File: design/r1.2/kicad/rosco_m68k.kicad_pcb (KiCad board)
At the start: 4 copper layers, 160 x 100 mm, 81 parts, among them IC1 MC68010P10, IC2 ATF16V8BQL-15PU, IC3 ATF16V8BQL, IC4 MC68901P, IC5 ATF16V8BQL, IC6 74174N, IC7 74LS93, IC8 555N, IC9 74LS01N, J1 PWR, J2 Conn_01x06, J3 Conn_02x32_Odd_Even, J5 GPIO-PANEL, Q1 3.6864MHz, Q2 5H8ET-10.000, Q3 5H8ET-4.000, U1 AT28C256-15PU, U2 AT28C256-15PU, U3 AS6C4008-55PCN, U4 AS6C4008-55PCN

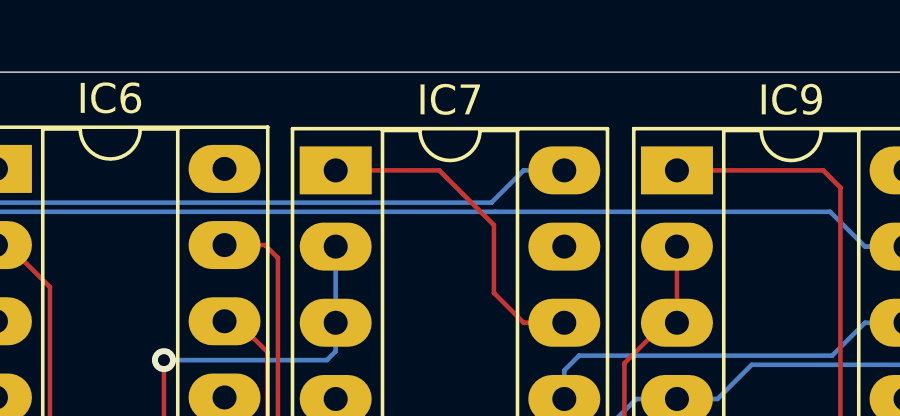
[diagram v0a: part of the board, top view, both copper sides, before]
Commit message: Rerate LED limiters for new LED stock
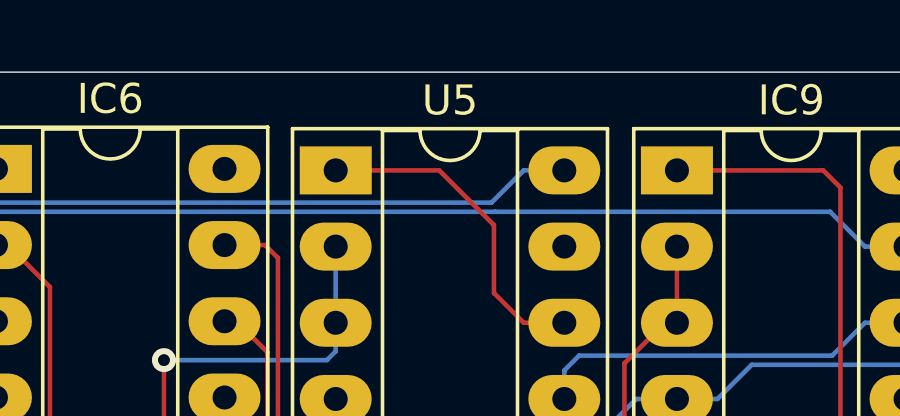
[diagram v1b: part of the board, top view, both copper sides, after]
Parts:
- IC3, IC5: value ATF16V8BQL -> ATF16V8BQL-15PU
- R1, R13: value 1K2 -> 330R
- renumbered IC7 to U5
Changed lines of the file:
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@@
   (net 121 "Net-(R12-Pad2)")
   (net 122 /Expansion/A17)
-  (net 123 "Net-(IC7-Pad1)")
-  (net 124 "Net-(IC7-Pad8)")
-  (net 125 "Net-(IC7-Pad9)")
-  (net 126 "Net-(IC7-Pad11)")
+  (net 123 "Net-(IC9-Pad11)")
+  (net 124 "Net-(U5-Pad1)")
+  (net 125 "Net-(U5-Pad8)")
+  (net 126 "Net-(U5-Pad9)")
   (net_class Default "This is the default net class."
     (clearance 0.1524)
@@
     (add_net "Net-(IC6-Pad2)")
     (add_net "Net-(IC6-Pad5)")
-    (add_net "Net-(IC7-Pad1)")
-    (add_net "Net-(IC7-Pad11)")
-    (add_net "Net-(IC7-Pad8)")
-    (add_net "Net-(IC7-Pad9)")
     (add_net "Net-(IC8-Pad3)")
     (add_net "Net-(IC8-Pad7)")
     (add_net "Net-(IC9-Pad10)")
+    (add_net "Net-(IC9-Pad11)")
     (add_net "Net-(J2-Pad3)")
     (add_net "Net-(J2-Pad6)")
@@
     (add_net "Net-(S1-Pad2)")
     (add_net "Net-(S1-Pad4)")
+    (add_net "Net-(U5-Pad1)")
+    (add_net "Net-(U5-Pad8)")
+    (add_net "Net-(U5-Pad9)")
     (add_net ODDRAMSEL)
     (add_net ODDROMSEL)
@@
     (descr "14-lead though-hole mounted DIP package, row spacing 7.62 mm (300 mils), Socket, LongPads")
     (tags "THT DIP DIL PDIP 2.54mm 7.62mm 300mil Socket LongPads")
-    (fp_text reference IC7 (at 3.81 -2.33) (layer F.SilkS)
+    (fp_text reference U5 (at 3.81 -2.33) (layer F.SilkS)
       (effects (font (size 1 1) (thickness 0.15)))
     )
@@
     )
     (pad 1 thru_hole rect (at 0 0) (size 2.4 1.6) (drill 0.8) (layers *.Cu *.Mask)
-      (net 123 "Net-(IC7-Pad1)"))
+      (net 124 "Net-(U5-Pad1)"))
     (pad 8 thru_hole oval (at 7.62 15.24) (size 2.4 1.6) (drill 0.8) (layers *.Cu *.Mask)
-      (net 124 "Net-(IC7-Pad8)"))
+      (net 125 "Net-(U5-Pad8)"))
     (pad 2 thru_hole oval (at 0 2.54) (size 2.4 1.6) (drill 0.8) (layers *.Cu *.Mask)
       (net 12 AS))
     (pad 9 thru_hole oval (at 7.62 12.7) (size 2.4 1.6) (drill 0.8) (layers *.Cu *.Mask)
-      (net 125 "Net-(IC7-Pad9)"))
+      (net 126 "Net-(U5-Pad9)"))
     (pad 3 thru_hole oval (at 0 5.08) (size 2.4 1.6) (drill 0.8) (layers *.Cu *.Mask)
       (net 12 AS))
@@
     (pad 4 thru_hole oval (at 0 7.62) (size 2.4 1.6) (drill 0.8) (layers *.Cu *.Mask))
     (pad 11 thru_hole oval (at 7.62 7.62) (size 2.4 1.6) (drill 0.8) (layers *.Cu *.Mask)
-      (net 126 "Net-(IC7-Pad11)"))
+      (net 123 "Net-(IC9-Pad11)"))
     (pad 5 thru_hole oval (at 0 10.16) (size 2.4 1.6) (drill 0.8) (layers *.Cu *.Mask)
       (net 17 VCC))
     (pad 12 thru_hole oval (at 7.62 5.08) (size 2.4 1.6) (drill 0.8) (layers *.Cu *.Mask)
-      (net 123 "Net-(IC7-Pad1)"))
+      (net 124 "Net-(U5-Pad1)"))
     (pad 6 thru_hole oval (at 0 12.7) (size 2.4 1.6) (drill 0.8) (layers *.Cu *.Mask))
     (pad 13 thru_hole oval (at 7.62 2.54) (size 2.4 1.6) (drill 0.8) (layers *.Cu *.Mask))
@@
       (net 7 RESET))
     (pad 11 thru_hole oval (at 7.62 7.62) (size 2.4 1.6) (drill 0.8) (layers *.Cu *.Mask)
-      (net 126 "Net-(IC7-Pad11)"))
+      (net 123 "Net-(IC9-Pad11)"))
     (pad 5 thru_hole oval (at 0 10.16) (size 2.4 1.6) (drill 0.8) (layers *.Cu *.Mask)
       (net 42 "Net-(IC8-Pad3)"))
     (pad 12 thru_hole oval (at 7.62 5.08) (size 2.4 1.6) (drill 0.8) (layers *.Cu *.Mask)
-      (net 126 "Net-(IC7-Pad11)"))
+      (net 123 "Net-(IC9-Pad11)"))
     (pad 6 thru_hole oval (at 0 12.7) (size 2.4 1.6) (drill 0.8) (layers *.Cu *.Mask)
       (net 42 "Net-(IC8-Pad3)"))
@@
       (effects (font (size 1.6891 1.6891) (thickness 0.16891)) (justify left bottom))
     )
-    (fp_text value ATF16V8BQL (at -10.16 0.762) (layer F.Fab)
+    (fp_text value ATF16V8BQL-15PU (at -10.16 0.762) (layer F.Fab)
       (effects (font (size 1.6891 1.6891) (thickness 0.16891)) (justify left bottom))
     )
@@
       (effects (font (size 1.2065 1.2065) (thickness 0.12065)) (justify right bottom))
     )
-    (fp_text value 1K2 (at -2.2606 0.635 90) (layer F.Fab)
+    (fp_text value 330R (at -2.2606 0.635 90) (layer F.Fab)
       (effects (font (size 1.2065 1.2065) (thickness 0.12065)) (justify right bottom))
     )
@@
       (effects (font (size 1.6891 1.6891) (thickness 0.16891)) (justify left bottom))
     )
-    (fp_text value ATF16V8BQL (at -10.16 0.762) (layer F.Fab)
+    (fp_text value ATF16V8BQL-15PU (at -10.16 0.762) (layer F.Fab)
       (effects (font (size 1.6891 1.6891) (thickness 0.16891)) (justify left bottom))
     )
@@
       (effects (font (size 1.2065 1.2065) (thickness 0.12065)) (justify left bottom))
     )
-    (fp_text value 1K2 (at 2.4384 -0.6096 90) (layer F.Fab)
+    (fp_text value 330R (at 2.4384 -0.6096 90) (layer F.Fab)
       (effects (font (size 1.2065 1.2065) (thickness 0.12065)) (justify left bottom))
     )
@@
   (segment (start 110.375 102.413) (end 110.398 102.39) (width 0.1524) (layer Top) (net 122))
   (segment (start 110.375 104.975) (end 110.375 102.413) (width 0.1524) (layer Top) (net 122))
-  (segment (start 192.0426 63.4548) (end 191.05 62.4622) (width 0.1524) (layer Top) (net 123))
-  (segment (start 193.395 63.4548) (end 192.0426 63.4548) (width 0.1524) (layer Top) (net 123))
-  (segment (start 191.05 62.4622) (end 191.05 60.2) (width 0.1524) (layer Top) (net 123))
-  (segment (start 189.2248 58.3748) (end 185.775 58.3748) (width 0.1524) (layer Top) (net 123))
-  (segment (start 191.05 60.2) (end 189.2248 58.3748) (width 0.1524) (layer Top) (net 123))
-  (segment (start 203.4176 63.4548) (end 202.3224 64.55) (width 0.1524) (layer Bottom) (net 126))
-  (segment (start 204.77 63.4548) (end 203.4176 63.4548) (width 0.1524) (layer Bottom) (net 126))
-  (segment (start 193.395 65.0424) (end 193.395 65.9948) (width 0.1524) (layer Bottom) (net 126))
-  (segment (start 193.8874 64.55) (end 193.395 65.0424) (width 0.1524) (layer Bottom) (net 126))
-  (segment (start 202.3224 64.55) (end 193.8874 64.55) (width 0.1524) (layer Bottom) (net 126))
-  (segment (start 204.77 64.4072) (end 204.77 65.9948) (width 0.1524) (layer Top) (net 126))
-  (segment (start 204.77 63.4548) (end 204.77 64.4072) (width 0.1524) (layer Top) (net 126))
+  (segment (start 192.0426 63.4548) (end 191.05 62.4622) (width 0.1524) (layer Top) (net 124))
+  (segment (start 193.395 63.4548) (end 192.0426 63.4548) (width 0.1524) (layer Top) (net 124))
+  (segment (start 191.05 62.4622) (end 191.05 60.2) (width 0.1524) (layer Top) (net 124))
+  (segment (start 189.2248 58.3748) (end 185.775 58.3748) (width 0.1524) (layer Top) (net 124))
+  (segment (start 191.05 60.2) (end 189.2248 58.3748) (width 0.1524) (layer Top) (net 124))
+  (segment (start 203.4176 63.4548) (end 202.3224 64.55) (width 0.1524) (layer Bottom) (net 123))
+  (segment (start 204.77 63.4548) (end 203.4176 63.4548) (width 0.1524) (layer Bottom) (net 123))
+  (segment (start 193.395 65.0424) (end 193.395 65.9948) (width 0.1524) (layer Bottom) (net 123))
+  (segment (start 193.8874 64.55) (end 193.395 65.0424) (width 0.1524) (layer Bottom) (net 123))
+  (segment (start 202.3224 64.55) (end 193.8874 64.55) (width 0.1524) (layer Bottom) (net 123))
+  (segment (start 204.77 64.4072) (end 204.77 65.9948) (width 0.1524) (layer Top) (net 123))
+  (segment (start 204.77 63.4548) (end 204.77 64.4072) (width 0.1524) (layer Top) (net 123))
   (zone (net 18) (net_name GND) (layer Route2) (hatch edge 0.508)
     (connect_pads (clearance 0.508))

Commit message: Update board for IC5 and tidy up
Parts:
- added J4: Conn_01x06, rosco_m68k:1X06, F.Cu at (223.3, 127.5)
- R21: value 4K7 -> 2K2
- moved C15 31.8 mm to (183.6, 102.0)
- moved C14 24.4 mm to (212.4, 106.7)
- moved C19 6.12 mm to (212.4, 100.1)
- moved J5 4.56 mm to (216.7, 131.3)
- moved C18 4.41 mm to (212.4, 93.5)
- moved LED3 0.53 mm to (210.4, 60.6), turned to 0 degrees
- renumbered U5 to IC7
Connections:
- IC5 pad 11: /Expansion/A17 -> /Expansion/A19
- IC5 pad 12: Net-(IC5-Pad12) -> MFPDS
- IC5 pad 14: DTACK -> Net-(IC5-Pad14)
- IC5 pad 15: MFPDS -> EXPSEL
- IC5 pad 19: Net-(IC5-Pad19) -> DTACK
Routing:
- net /Expansion/A17: track 241.3 -> 201.1 mm, vias 7 -> 6
- net /Expansion/A19: track 193.8 -> 214.0 mm, vias 4 -> 5
- net DTACK: track 162.4 -> 175.5 mm
- net TBI: track 63.6 -> 52.4 mm
- net LDS: track 94.0 -> 104.8 mm
- net TAO: track 36.5 -> 27.5 mm, vias 1 -> 0
- net TAI: track 61.2 -> 52.9 mm
- net EXPSEL: track 178.4 -> 186.4 mm, vias 5 -> 6
- net TBO: track 42.7 -> 35.0 mm, vias 1 -> 0
- net MFPDS: track 113.2 -> 105.9 mm
- net Net-(IC9-Pad10): track 10.3 -> 16.3 mm
- net EVENRAMSEL: track 210.4 -> 204.7 mm
- net GPIO5: track 37.5 -> 32.9 mm
- net ODDRAMSEL: track 213.5 -> 209.0 mm
- net EVENROMSEL: track 214.8 -> 210.3 mm
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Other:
- board text added: "16"
- board text added: "CS SCK MOSI MISO VCC GND"
- board text added: "I/O"
- board text added: "RESET"
- board text added: "RUN"
- board text added: "Revision 1.23 (April 2021)"
- board text removed: "IO & PANEL"
- board text removed: "RUN RESET"
- board text removed: "Revision 1.2 (August 2020)"

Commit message: Silkscreen tweaks for manufacturing
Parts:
- added REF**: WEEE-Logo_4.2x6mm_SilkScreen, Symbol:WEEE-Logo_4.2x6mm_SilkScreen, B.Cu at (92.2, 76.3)
- added REF**: RoHS-Logo_6mm_SilkScreen, Symbol:RoHS-Logo_6mm_SilkScreen, B.Cu at (92.2, 68.2)
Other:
- board text added: "Copyright ©2021"
- board text added: "First Anniversary Edition"
- board text added: "revision 1.23"
- board text added: "rosco_m68k"
- board text removed: "Copyright ©2020"
- board text removed: "rosco_m68k revision 1.2"
